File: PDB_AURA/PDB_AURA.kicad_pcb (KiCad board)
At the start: 4 copper layers, 50 x 50 mm, 85 parts, among them J100 XT30PW-M, J300 XT30PW-F, J301 XT30PW-F, J302 532617012, J303 XT30PW-F, J304 XT30PW-F, Q100 CSD18540Q5B, Q200 CSD18540Q5B, Q201 CSD18510Q5B, Q300 HSK10N06, Q301 HSK10N06, U100 LM74700, U200 LM25145RGYR, U300 LTV-217-B-G, U301 LTV-217-B-G, U302 INA219AIDCNR

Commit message: Second iteration PDB
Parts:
- C212: value 2n2 -> 1n
- C216: value 22u -> 47u
- R207: value 680R -> 1k
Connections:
- H100 pad 1: unconnected-(H100-Pad1) -> GND
- H101 pad 1: unconnected-(H101-Pad1)_6 -> GND
- H102 pad 1: unconnected-(H102-Pad1)_1 -> GND
- H103 pad 1: unconnected-(H103-Pad1)_7 -> GND
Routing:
- net +5V: track 72.4 -> 80.1 mm, vias 19 -> 35
- net GND: vias 276 -> 280
- net INA_IN+: vias 38 -> 55

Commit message: PDB organised
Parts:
- C207: footprint Resistor_SMD:R_0402_1005Metric -> Capacitor_SMD:C_0402_1005Metric
- C210: value 27p -> 10p
- R205: value 1k -> 2k
- R206: value 5k1 -> 10k5
- R210: value 220R -> 470R
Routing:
- net +5V: track 80.1 -> 72.6 mm
- net GND: vias 280 -> 283
- net +BATT_FILT: vias 194 -> 204

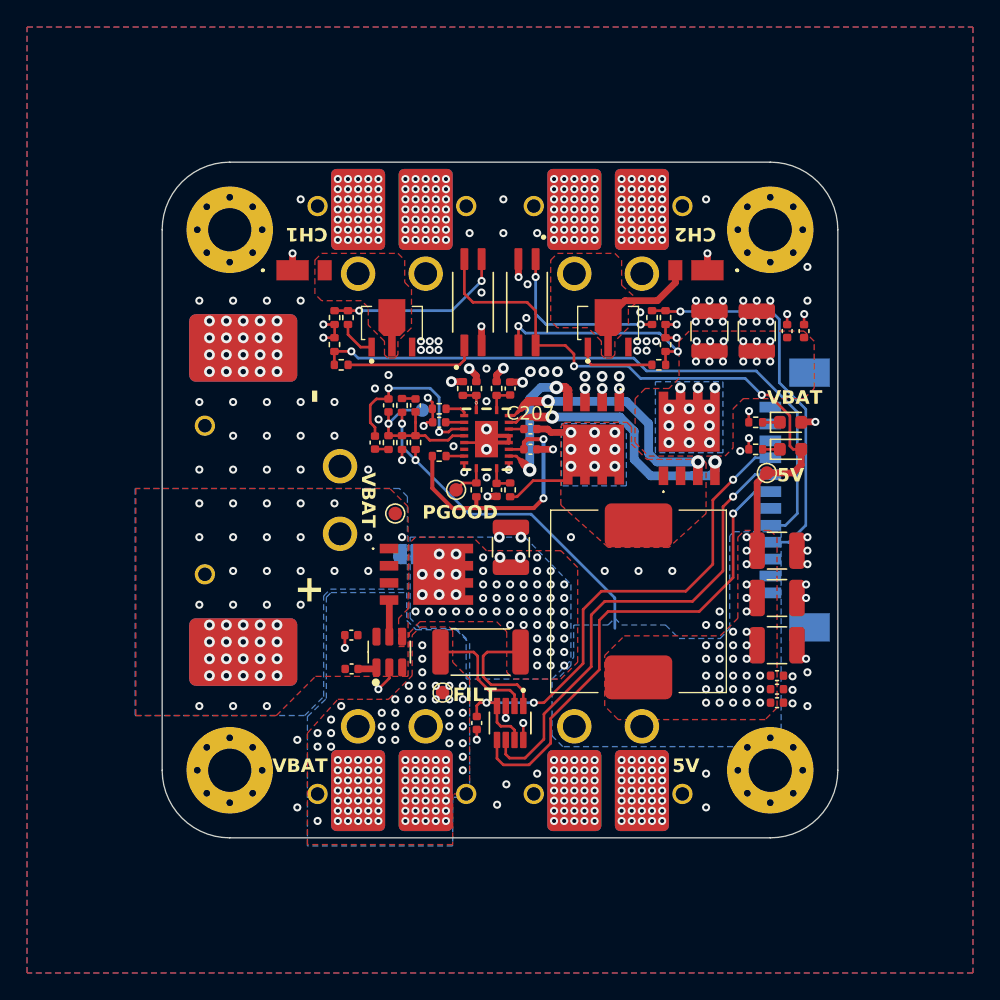
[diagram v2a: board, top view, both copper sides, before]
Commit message: Silk Screen Done
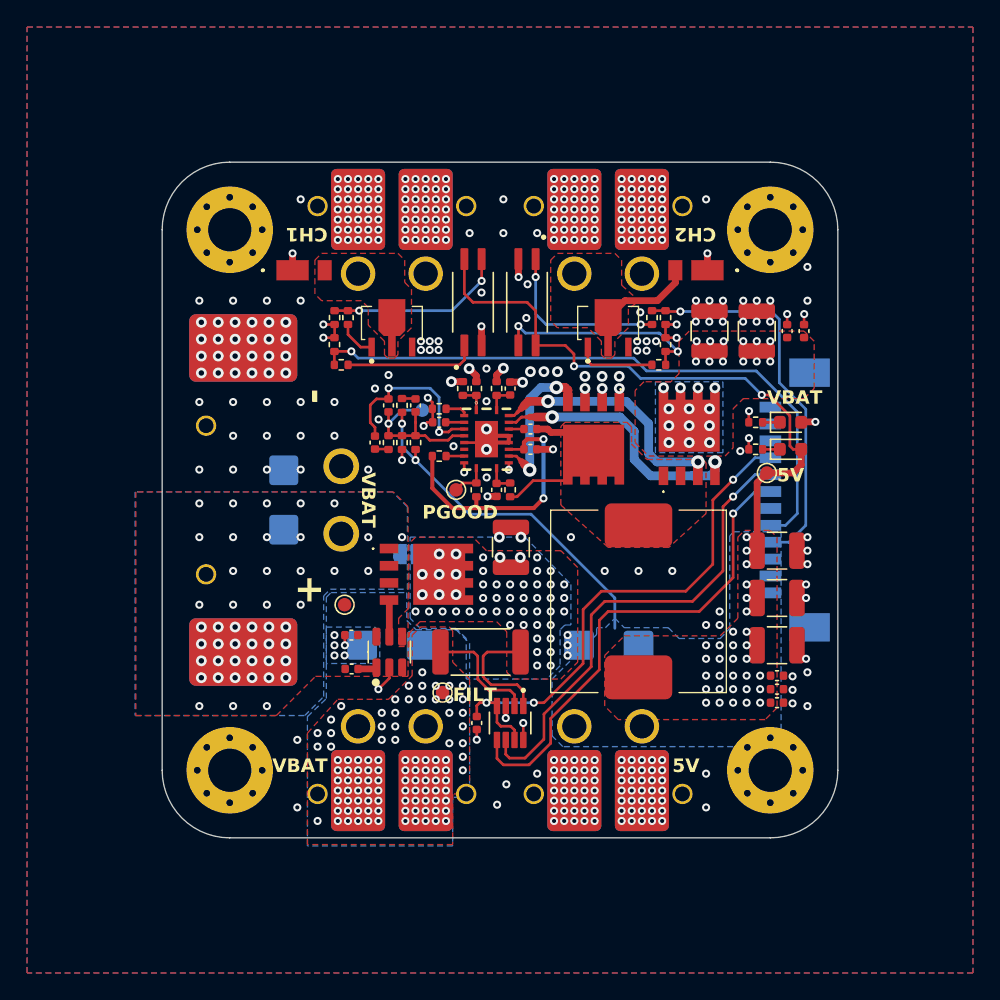
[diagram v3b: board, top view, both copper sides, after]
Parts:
- added D101: SMBJ33CA, SMBJ33CA:DIONM5436X244N, B.Cu at (59.0, 75.0)
- added D304: SMBJ33CA, SMBJ33CA:DIONM5436X244N, B.Cu at (67.0, 85.8)
- added D305: SMBJ33CA, SMBJ33CA:DIONM5436X244N, B.Cu at (83.0, 85.8)
- moved TP100 7.72 mm to (63.5, 82.8)
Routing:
- net GND: track 31.4 -> 31.2 mm, vias 283 -> 294
- net INA_IN+: vias 55 -> 51
- net /200_Buck_Regulator/5V_SW: vias 11 -> 2
- net +BATT_FILT: vias 204 -> 202
- net +BATT: vias 43 -> 47
- removed copper zone on B.Cu, net /200_Buck_Regulator/5V_SW
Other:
- board text added: "AURA PDB"
- board text added: "Alexander Armitage"
- board text added: "V0.0.1"

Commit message: First Order
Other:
- board text added: "V1.0"
- board text removed: "V0.0.1"
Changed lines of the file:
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@@
 		)
 	)
-	(gr_text "V0.0.1"
+	(gr_text "V1.0"
 		(at 80.25 75.25 90)
 		(layer "B.SilkS")
@@
 			(pts
 				(xy 95.75 77.35) (xy 95.8 77.35) (xy 95.8 93.25) (xy 79.65 93.25) (xy 78.85 92.45) (xy 78.85 88.25)
-				(xy 82.15 84.95) (xy 82.15 84.45) (xy 82.8 84.45) (xy 83.5 83.75) (xy 84.2 84.45) (xy 87.45 84.45)
+				(xy 82.2 84.9) (xy 82.2 84.45) (xy 82.8 84.45) (xy 83.5 83.75) (xy 84.2 84.45) (xy 87.45 84.45)
 				(xy 88.25 85.25) (xy 91.3 85.25) (xy 92 84.5) (xy 92 77.65) (xy 92.3 77.35)
 			)
